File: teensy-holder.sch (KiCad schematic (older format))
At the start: 16 parts, among them P1 BNC, P2 A1, P3 A2, U1 Teensy3.2_DIP

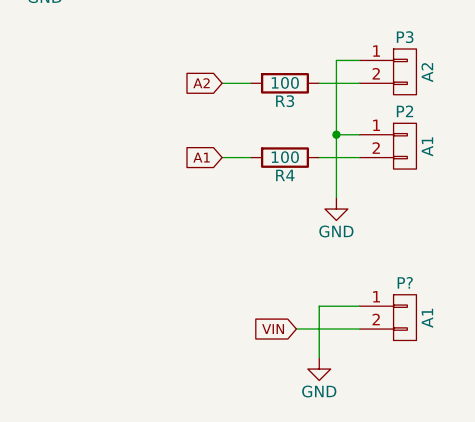
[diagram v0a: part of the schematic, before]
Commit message: Added more parts, started board layout
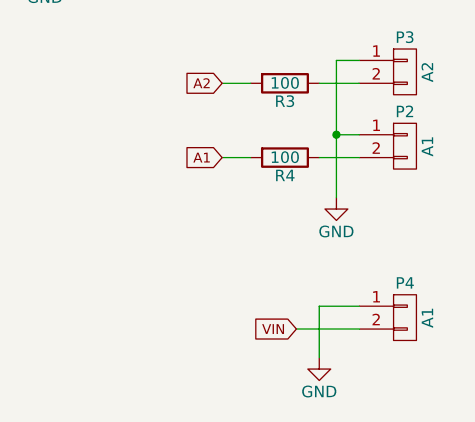
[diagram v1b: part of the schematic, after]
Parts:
- D1, D2, D3, D4, D5, D6: footprint (none) -> visgence_parts:SOD-323
- P2, P3: footprint (none) -> visgence_parts:Term3.5-2
- P4: renamed from P?; footprint (none) -> visgence_parts:Term3.5-2
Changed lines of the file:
@@
 encoding utf-8
 Sheet 1 1
-Title ""
+Title "Teensy Holder"
 Date ""
 Rev ""
-Comp ""
+Comp "Visgence Inc"
 Comment1 ""
 Comment2 ""
@@
 F 0 "D1" H 5250 2000 50  0000 C CNN
 F 1 "D" H 5250 1800 50  0000 C CNN
-F 2 "" H 5250 1900 50  0000 C CNN
+F 2 "visgence_parts:SOD-323" H 5250 1900 50  0001 C CNN
 F 3 "" H 5250 1900 50  0000 C CNN
 	1    5250 1900
@@
 F 0 "D2" H 5250 2550 50  0000 C CNN
 F 1 "D" H 5250 2350 50  0000 C CNN
-F 2 "" H 5250 2450 50  0000 C CNN
+F 2 "visgence_parts:SOD-323" H 5250 2450 50  0001 C CNN
 F 3 "" H 5250 2450 50  0000 C CNN
 	1    5250 2450
@@
 F 0 "D3" H 6700 2025 50  0000 C CNN
 F 1 "D" H 6700 1825 50  0000 C CNN
-F 2 "" H 6700 1925 50  0000 C CNN
+F 2 "visgence_parts:SOD-323" H 6700 1925 50  0001 C CNN
 F 3 "" H 6700 1925 50  0000 C CNN
 	1    6700 1925
@@
 F 0 "D4" H 6700 2500 50  0000 C CNN
 F 1 "D" H 6700 2300 50  0000 C CNN
-F 2 "" H 6700 2400 50  0000 C CNN
+F 2 "visgence_parts:SOD-323" H 6700 2400 50  0001 C CNN
 F 3 "" H 6700 2400 50  0000 C CNN
 	1    6700 2400
@@
 F 0 "D5" H 7175 2025 50  0000 C CNN
 F 1 "D" H 7175 1825 50  0000 C CNN
-F 2 "" H 7175 1925 50  0000 C CNN
+F 2 "visgence_parts:SOD-323" H 7175 1925 50  0001 C CNN
 F 3 "" H 7175 1925 50  0000 C CNN
 	1    7175 1925
@@
 F 0 "D6" H 7175 2500 50  0000 C CNN
 F 1 "D" H 7175 2300 50  0000 C CNN
-F 2 "" H 7175 2400 50  0000 C CNN
+F 2 "visgence_parts:SOD-323" H 7175 2400 50  0001 C CNN
 F 3 "" H 7175 2400 50  0000 C CNN
 	1    7175 2400
@@
 A2
 $Comp
-L GND #PWR10
+L GND #PWR11
 U 1 1 5885D122
 P 7175 2675
-F 0 "#PWR10" H 7175 2425 50  0001 C CNN
+F 0 "#PWR11" H 7175 2425 50  0001 C CNN
 F 1 "GND" H 7175 2525 50  0000 C CNN
 F 2 "" H 7175 2675 50  0000 C CNN
@@
 	6700 1675 6700 1775
 $Comp
-L +3.3V #PWR9
+L +3.3V #PWR10
 U 1 1 5885D3BA
 P 7175 1675
-F 0 "#PWR9" H 7175 1525 50  0001 C CNN
+F 0 "#PWR10" H 7175 1525 50  0001 C CNN
 F 1 "+3.3V" H 7175 1815 50  0000 C CNN
 F 2 "" H 7175 1675 50  0000 C CNN
@@
 F 0 "P2" H 7100 3725 50  0000 C CNN
 F 1 "A1" V 7200 3575 50  0000 C CNN
-F 2 "" H 7100 3575 50  0000 C CNN
+F 2 "visgence_parts:Term3.5-2" H 7100 3575 50  0001 C CNN
 F 3 "" H 7100 3575 50  0000 C CNN
 	1    7100 3575
@@
 	6725 3625 6900 3625
 $Comp
-L GND #PWR8
+L GND #PWR9
 U 1 1 5885E0A6
 P 6800 3800
-F 0 "#PWR8" H 6800 3550 50  0001 C CNN
+F 0 "#PWR9" H 6800 3550 50  0001 C CNN
 F 1 "GND" H 6800 3650 50  0000 C CNN
 F 2 "" H 6800 3800 50  0000 C CNN
@@
 F 0 "P3" H 7100 3400 50  0000 C CNN
 F 1 "A2" V 7200 3250 50  0000 C CNN
-F 2 "" H 7100 3250 50  0000 C CNN
+F 2 "visgence_parts:Term3.5-2" H 7100 3250 50  0001 C CNN
 F 3 "" H 7100 3250 50  0000 C CNN
 	1    7100 3250
@@
 	6425 3625 6300 3625
 $Comp
-L CONN_01X02 P?
+L CONN_01X02 P4
 U 1 1 5886131A
 P 7100 4325
-F 0 "P?" H 7100 4475 50  0000 C CNN
+F 0 "P4" H 7100 4475 50  0000 C CNN
 F 1 "A1" V 7200 4325 50  0000 C CNN
-F 2 "" H 7100 4325 50  0000 C CNN
+F 2 "visgence_parts:Term3.5-2" H 7100 4325 50  0001 C CNN
 F 3 "" H 7100 4325 50  0000 C CNN
 	1    7100 4325
@@
 $EndComp
 $Comp
-L GND #PWR?
+L GND #PWR8
 U 1 1 58861908
 P 6725 4500
-F 0 "#PWR?" H 6725 4250 50  0001 C CNN
+F 0 "#PWR8" H 6725 4250 50  0001 C CNN
 F 1 "GND" H 6725 4350 50  0000 C CNN
 F 2 "" H 6725 4500 50  0000 C CNN

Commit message: board layout
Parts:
- D1, D2, D3, D4, D5, D6: footprint visgence_parts:SOD-323 -> Diodes_SMD:D_SOD-323_HandSoldering
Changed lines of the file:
@@
 $EndComp
 $Comp
-L GND #PWR1
+L GND #PWR01
 U 1 1 58858AE0
 P 1675 1625
-F 0 "#PWR1" H 1675 1375 50  0001 C CNN
+F 0 "#PWR01" H 1675 1375 50  0001 C CNN
 F 1 "GND" H 1675 1475 50  0000 C CNN
 F 2 "" H 1675 1625 50  0000 C CNN
@@
 	5825 2175 5900 2175
 $Comp
-L +3.3V #PWR2
+L +3.3V #PWR02
 U 1 1 588597A8
 P 4375 1675
-F 0 "#PWR2" H 4375 1525 50  0001 C CNN
+F 0 "#PWR02" H 4375 1525 50  0001 C CNN
 F 1 "+3.3V" H 4375 1815 50  0000 C CNN
 F 2 "" H 4375 1675 50  0000 C CNN
@@
 	4375 1750 4375 1675
 $Comp
-L +3.3V #PWR3
+L +3.3V #PWR03
 U 1 1 58859887
 P 5525 1575
-F 0 "#PWR3" H 5525 1425 50  0001 C CNN
+F 0 "#PWR03" H 5525 1425 50  0001 C CNN
 F 1 "+3.3V" H 5525 1715 50  0000 C CNN
 F 2 "" H 5525 1575 50  0000 C CNN
@@
 $EndComp
 $Comp
-L GND #PWR4
+L GND #PWR04
 U 1 1 58859910
 P 5525 2775
-F 0 "#PWR4" H 5525 2525 50  0001 C CNN
+F 0 "#PWR04" H 5525 2525 50  0001 C CNN
 F 1 "GND" H 5525 2625 50  0000 C CNN
 F 2 "" H 5525 2775 50  0000 C CNN
@@
 	5525 2025 5525 2300
 $Comp
-L GND #PWR5
+L GND #PWR05
 U 1 1 58859DC1
 P 6050 2500
-F 0 "#PWR5" H 6050 2250 50  0001 C CNN
+F 0 "#PWR05" H 6050 2250 50  0001 C CNN
 F 1 "GND" H 6050 2350 50  0000 C CNN
 F 2 "" H 6050 2500 50  0000 C CNN
@@
 F 0 "D1" H 5250 2000 50  0000 C CNN
 F 1 "D" H 5250 1800 50  0000 C CNN
-F 2 "visgence_parts:SOD-323" H 5250 1900 50  0001 C CNN
+F 2 "Diodes_SMD:D_SOD-323_HandSoldering" H 5250 1900 50  0001 C CNN
 F 3 "" H 5250 1900 50  0000 C CNN
 	1    5250 1900
@@
 F 0 "D2" H 5250 2550 50  0000 C CNN
 F 1 "D" H 5250 2350 50  0000 C CNN
-F 2 "visgence_parts:SOD-323" H 5250 2450 50  0001 C CNN
+F 2 "Diodes_SMD:D_SOD-323_HandSoldering" H 5250 2450 50  0001 C CNN
 F 3 "" H 5250 2450 50  0000 C CNN
 	1    5250 2450
@@
 F 0 "D3" H 6700 2025 50  0000 C CNN
 F 1 "D" H 6700 1825 50  0000 C CNN
-F 2 "visgence_parts:SOD-323" H 6700 1925 50  0001 C CNN
+F 2 "Diodes_SMD:D_SOD-323_HandSoldering" H 6700 1925 50  0001 C CNN
 F 3 "" H 6700 1925 50  0000 C CNN
 	1    6700 1925
@@
 F 0 "D4" H 6700 2500 50  0000 C CNN
 F 1 "D" H 6700 2300 50  0000 C CNN
-F 2 "visgence_parts:SOD-323" H 6700 2400 50  0001 C CNN
+F 2 "Diodes_SMD:D_SOD-323_HandSoldering" H 6700 2400 50  0001 C CNN
 F 3 "" H 6700 2400 50  0000 C CNN
 	1    6700 2400
@@
 A1
 $Comp
-L GND #PWR7
+L GND #PWR06
 U 1 1 5885C3EF
 P 6700 2675
-F 0 "#PWR7" H 6700 2425 50  0001 C CNN
+F 0 "#PWR06" H 6700 2425 50  0001 C CNN
 F 1 "GND" H 6700 2525 50  0000 C CNN
 F 2 "" H 6700 2675 50  0000 C CNN
@@
 F 0 "D5" H 7175 2025 50  0000 C CNN
 F 1 "D" H 7175 1825 50  0000 C CNN
-F 2 "visgence_parts:SOD-323" H 7175 1925 50  0001 C CNN
+F 2 "Diodes_SMD:D_SOD-323_HandSoldering" H 7175 1925 50  0001 C CNN
 F 3 "" H 7175 1925 50  0000 C CNN
 	1    7175 1925
@@
 F 0 "D6" H 7175 2500 50  0000 C CNN
 F 1 "D" H 7175 2300 50  0000 C CNN
-F 2 "visgence_parts:SOD-323" H 7175 2400 50  0001 C CNN
+F 2 "Diodes_SMD:D_SOD-323_HandSoldering" H 7175 2400 50  0001 C CNN
 F 3 "" H 7175 2400 50  0000 C CNN
 	1    7175 2400
@@
 A2
 $Comp
-L GND #PWR11
+L GND #PWR07
 U 1 1 5885D122
 P 7175 2675
-F 0 "#PWR11" H 7175 2425 50  0001 C CNN
+F 0 "#PWR07" H 7175 2425 50  0001 C CNN
 F 1 "GND" H 7175 2525 50  0000 C CNN
 F 2 "" H 7175 2675 50  0000 C CNN
@@
 	7175 2150 7000 2150
 $Comp
-L +3.3V #PWR6
+L +3.3V #PWR08
 U 1 1 5885D35E
 P 6700 1675
-F 0 "#PWR6" H 6700 1525 50  0001 C CNN
+F 0 "#PWR08" H 6700 1525 50  0001 C CNN
 F 1 "+3.3V" H 6700 1815 50  0000 C CNN
 F 2 "" H 6700 1675 50  0000 C CNN
@@
 	6700 1675 6700 1775
 $Comp
-L +3.3V #PWR10
+L +3.3V #PWR09
 U 1 1 5885D3BA
 P 7175 1675
-F 0 "#PWR10" H 7175 1525 50  0001 C CNN
+F 0 "#PWR09" H 7175 1525 50  0001 C CNN
 F 1 "+3.3V" H 7175 1815 50  0000 C CNN
 F 2 "" H 7175 1675 50  0000 C CNN
@@
 	6725 3625 6900 3625
 $Comp
-L GND #PWR9
+L GND #PWR010
 U 1 1 5885E0A6
 P 6800 3800
-F 0 "#PWR9" H 6800 3550 50  0001 C CNN
+F 0 "#PWR010" H 6800 3550 50  0001 C CNN
 F 1 "GND" H 6800 3650 50  0000 C CNN
 F 2 "" H 6800 3800 50  0000 C CNN
@@
 $EndComp
 $Comp
-L GND #PWR8
+L GND #PWR011
 U 1 1 58861908
 P 6725 4500
-F 0 "#PWR8" H 6725 4250 50  0001 C CNN
+F 0 "#PWR011" H 6725 4250 50  0001 C CNN
 F 1 "GND" H 6725 4350 50  0000 C CNN
 F 2 "" H 6725 4500 50  0000 C CNN

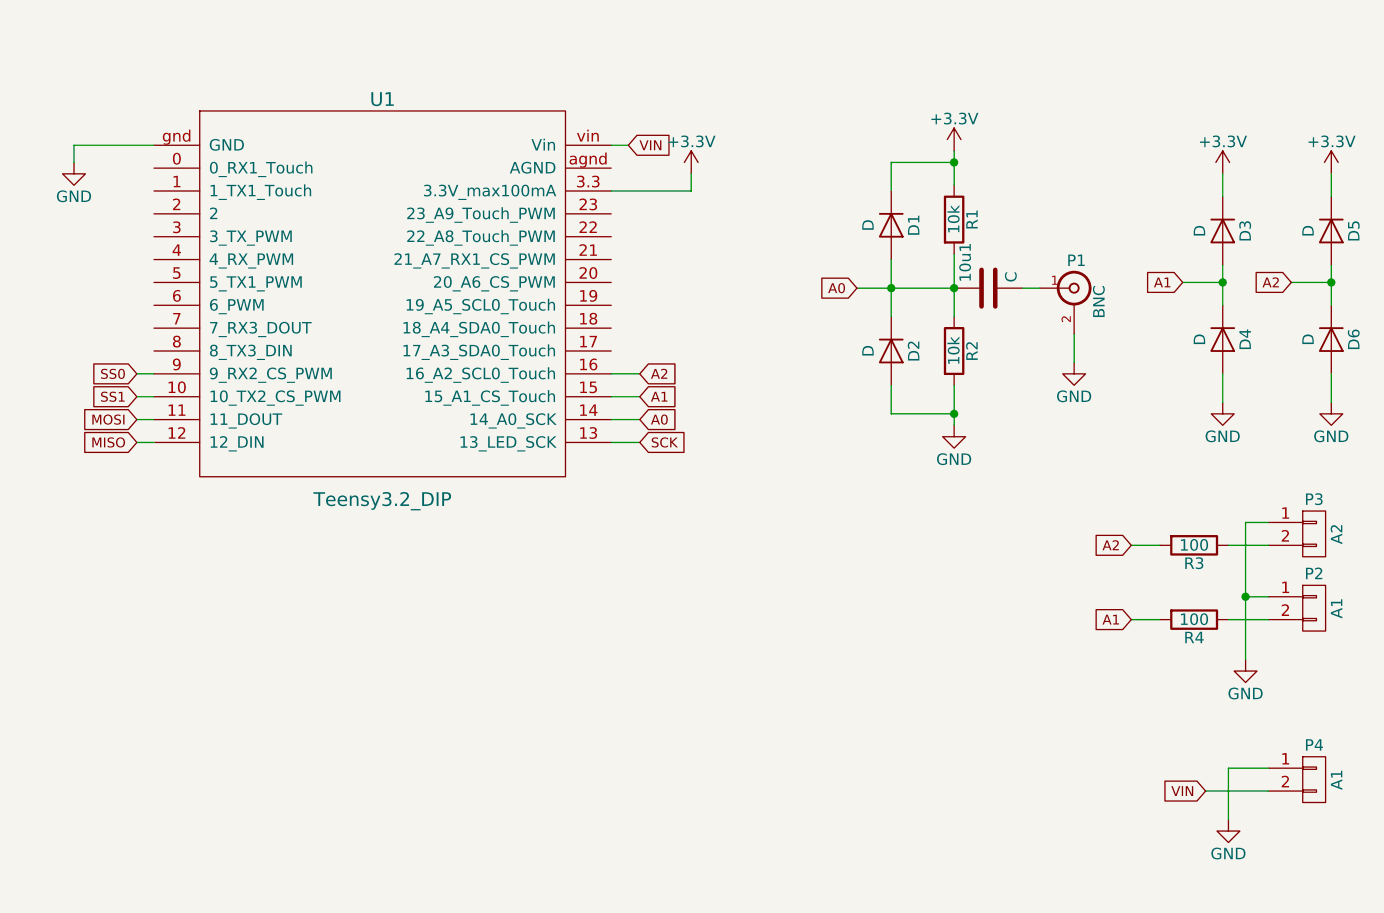
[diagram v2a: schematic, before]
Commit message: Added 3.3v to term at bottom
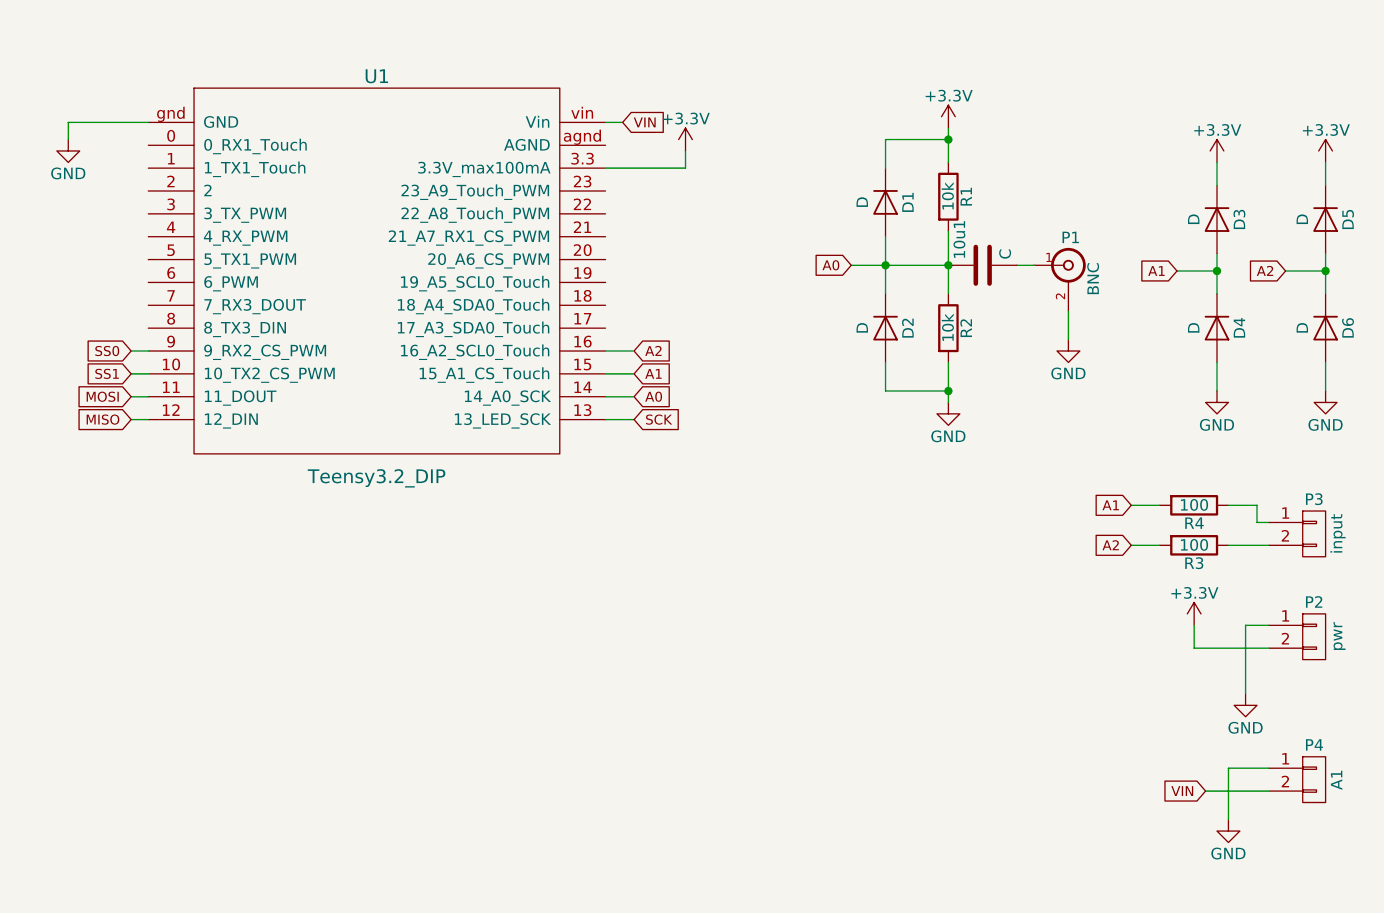
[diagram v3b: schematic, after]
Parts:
- P2: value A1 -> pwr
- P3: value A2 -> input
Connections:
- net +3V3: now also P2.2 (P2)
- net GND: no longer P3.1 (P1)
- net at R4.1: now also P3.1 (P1); no longer P2.2 (P2)
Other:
- moved on the sheet: 10u1, D1, D2, D3, D4, D5, D6, P1, R1, R2, R4, U1

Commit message: Added more ports, did some layout, swaped diodes
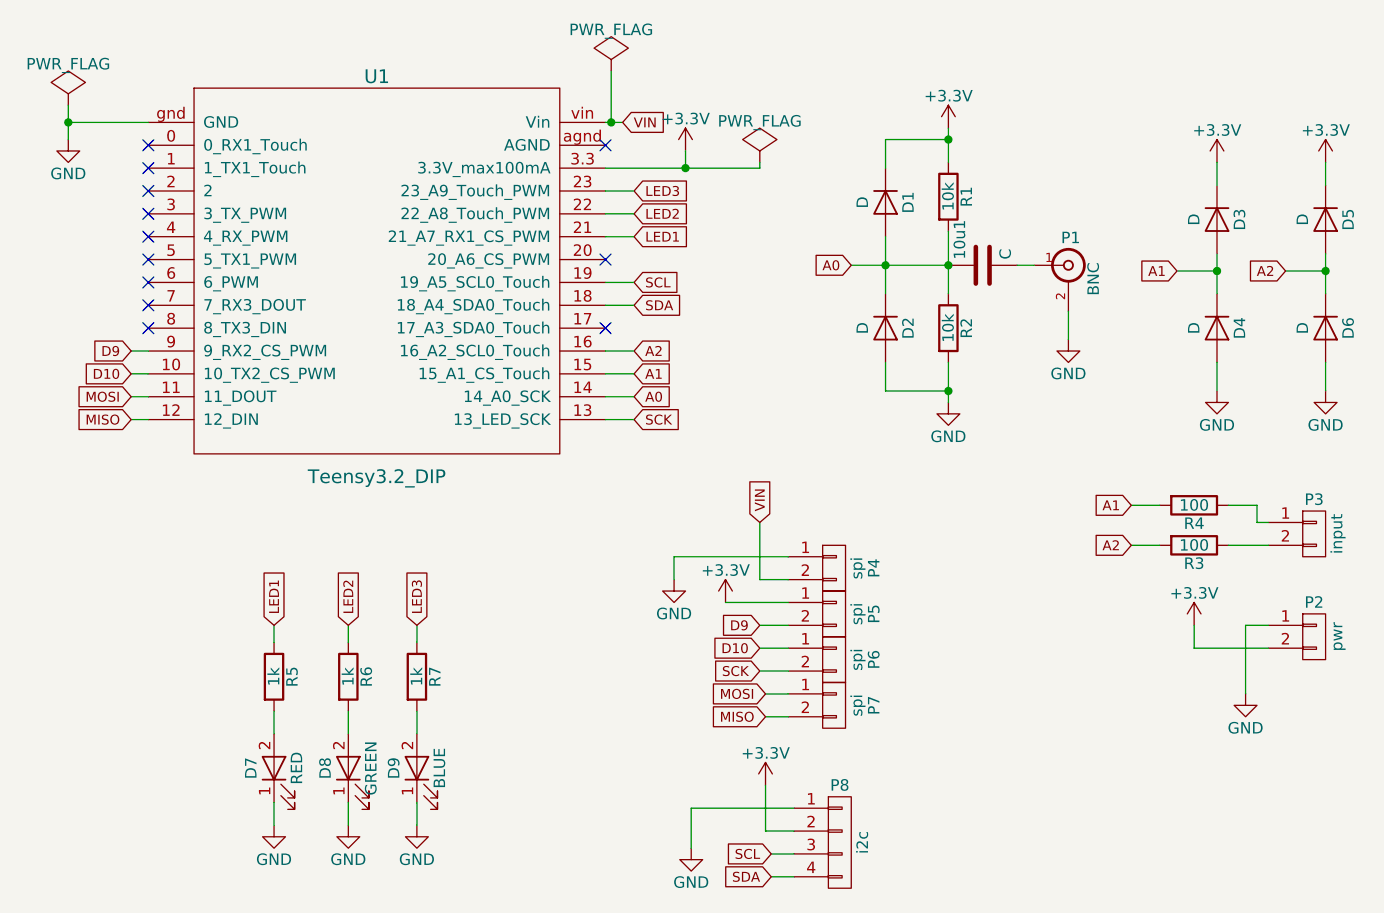
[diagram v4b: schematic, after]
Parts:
- added D7: RED, LEDs:LED_0603, symbol LED
- added D8: GREEN, LEDs:LED_0603, symbol LED
- added D9: BLUE, LEDs:LED_0603, symbol LED
- added P5, P6, P7: spi, visgence_parts:Term3.5-2, symbol CONN_01X02
- added P8: i2c, Pin_Headers:Pin_Header_Straight_1x04_Pitch2.54mm, symbol CONN_01X04
- added R5, R6, R7: 1k, visgence_parts:SM0603_VIS, symbol R
- D1, D2, D3, D4, D5, D6: footprint Diodes_SMD:D_SOD-323_HandSoldering -> Diodes_SMD:D_SOD-323
- P4: value A1 -> spi
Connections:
- net +3V3: now also P5.1 (P1), P8.2 (P2)
- net GND: now also D7.1 (K), D8.1 (K), D9.1 (K), P8.1 (P1)
- net MISO: now also P7.2 (P2)
- net MOSI: now also P7.1 (P1)
- net SCK: now also P6.2 (P2)
- net SDA: now reaches U1.18 (18_A4_SDA0_Touch)
- net SDA: now also P8.4 (P4)
- net SCL: now reaches U1.19 (19_A5_SCL0_Touch)
- net SCL: now also P8.3 (P3)
- net LED1: now reaches U1.21 (21_A7_RX1_CS_PWM)
- net LED1: now also R5.1
- net LED2: now reaches U1.22 (22_A8_Touch_PWM)
- net LED2: now also R6.1
- net LED3: now reaches U1.23 (23_A9_Touch_PWM)
- net LED3: now also R7.1
- net SS0 renamed D9
- net D9: now also P5.2 (P2)
- net SS1 renamed D10
- net D10: now also P6.1 (P1)
- new net: D7.2 (A), R5.2
- new net: D8.2 (A), R6.2
- new net: D9.2 (A), R7.2
- no-connect marks 0 -> 12
